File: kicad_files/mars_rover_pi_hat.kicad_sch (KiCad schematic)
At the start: 22 parts, among them IC1 DRV8825PWPR, J1 Conn_01x04, J2 Conn_01x03, J3 Conn_01x03, J4 Conn_01x04, J5 Conn_01x04, J6 Conn_01x03, J8 Conn_01x04, J9 Conn_02x20_Odd_Even

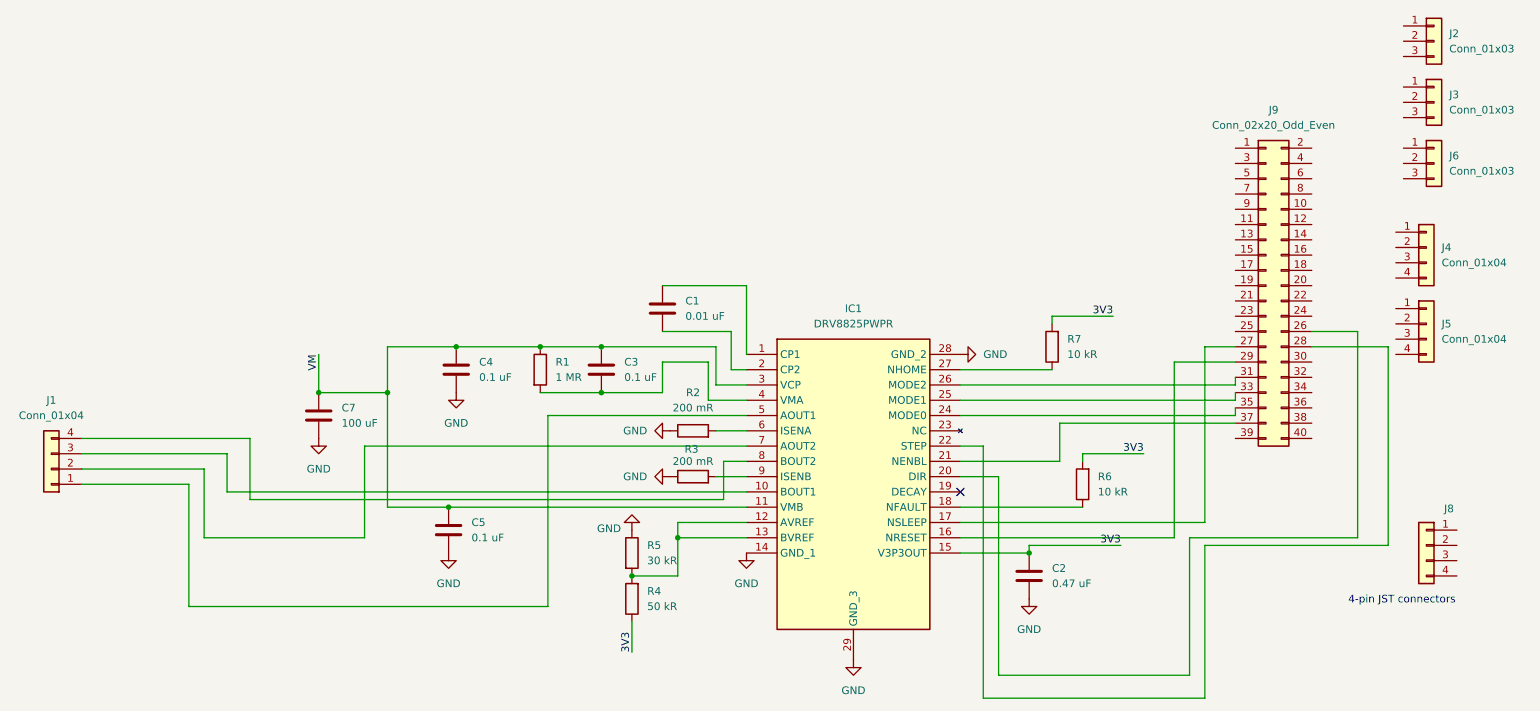
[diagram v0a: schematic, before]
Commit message: started hierarchical sheet for drv
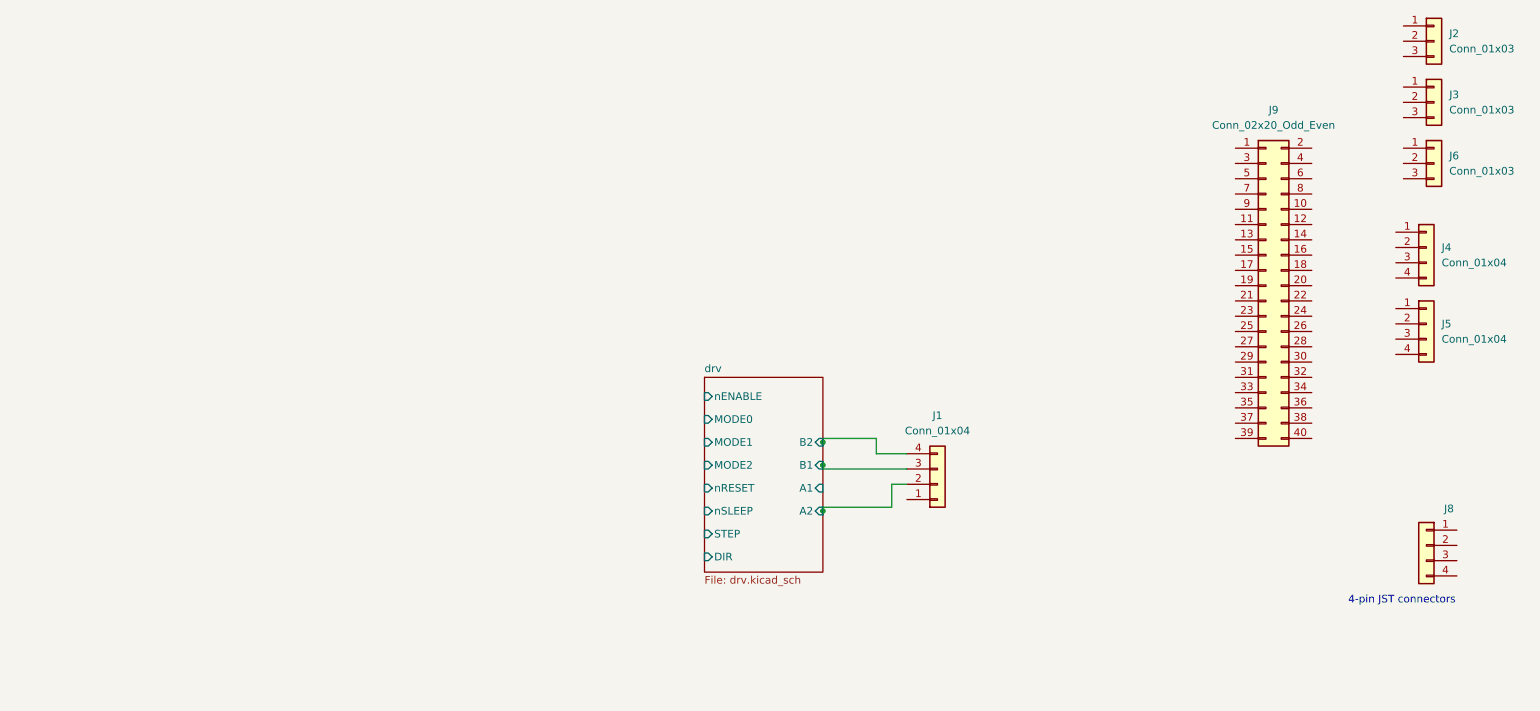
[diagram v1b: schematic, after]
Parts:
- removed C1: 0.01 uF, symbol Device:C
- removed C2: 0.47 uF, symbol Device:C
- removed C3, C4, C5: 0.1 uF, symbol Device:C
- removed C7: 100 uF, symbol Device:C
- removed IC1: DRV8825PWPR, SOP65P640X120-29N, symbol pi_hat:DRV8825PWPR
- removed R1: 1 MR, symbol Device:R
- removed R2, R3: 200 mR, symbol Device:R
- removed R4: 50 kR, symbol Device:R
- removed R5: 30 kR, symbol Device:R
- removed R6, R7: 10 kR, symbol Device:R
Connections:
- net drv/B1: now reaches J1.3 (Pin_3)
- net drv/A2: now reaches J1.2 (Pin_2)
- net drv/B2: now reaches J1.4 (Pin_4)
- no-connect marks 1 -> 0
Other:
- added sheet drv (drv.kicad_sch)
- moved on the sheet: J1
